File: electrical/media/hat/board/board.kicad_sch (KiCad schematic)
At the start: 9 parts, among them J101 RPI_PINS, J102 5V_IN, SW101 TS50810-411-02528

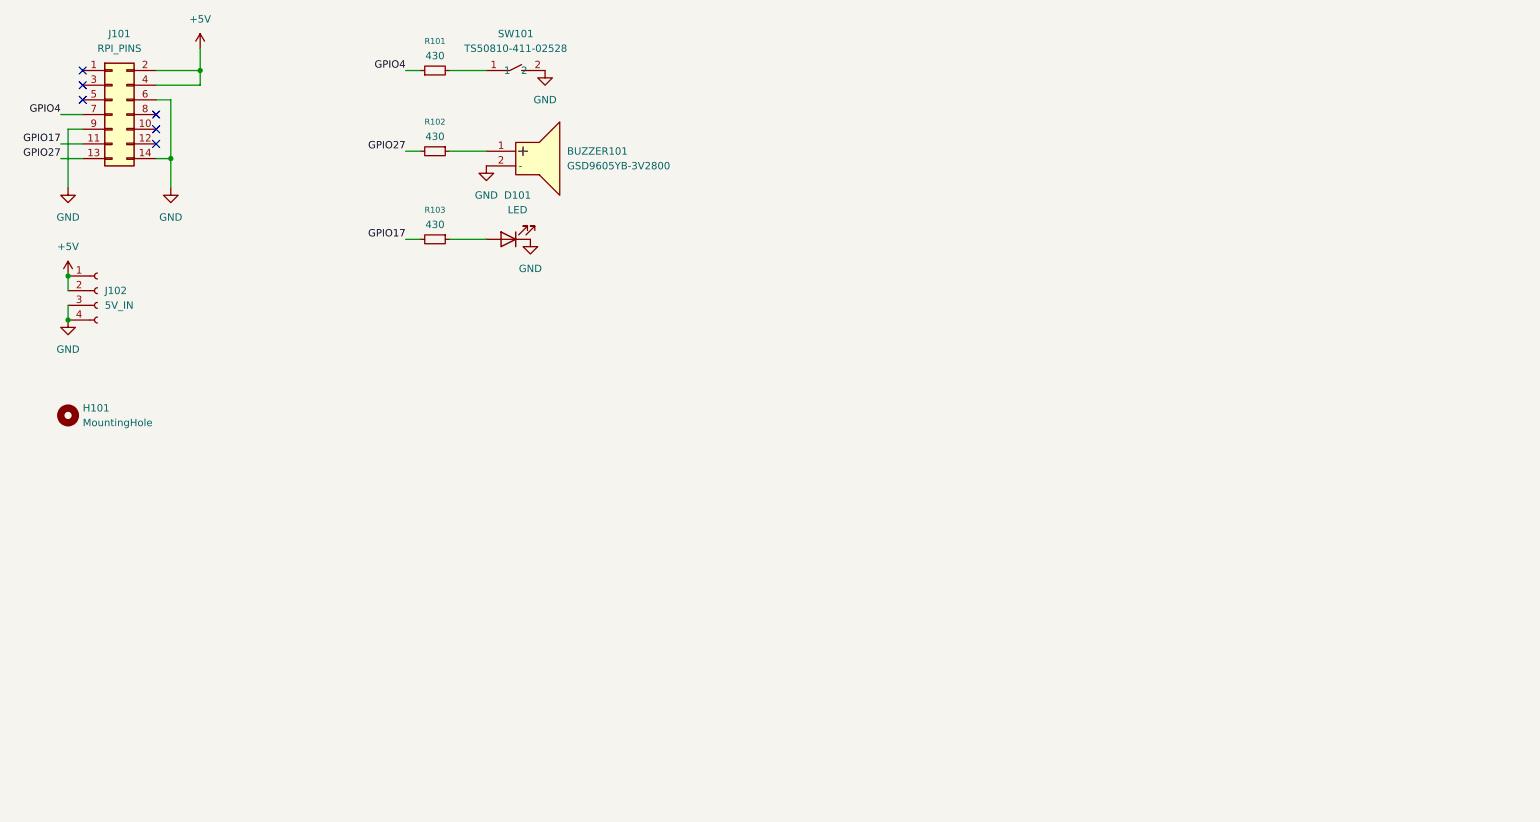
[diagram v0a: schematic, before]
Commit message: media hat power fix fabrication ready (#22)
* media hat power fix fabrication ready

* fix  STEP path

* flip connector polarity

* change FLT to RED LED

* LCSC number fix
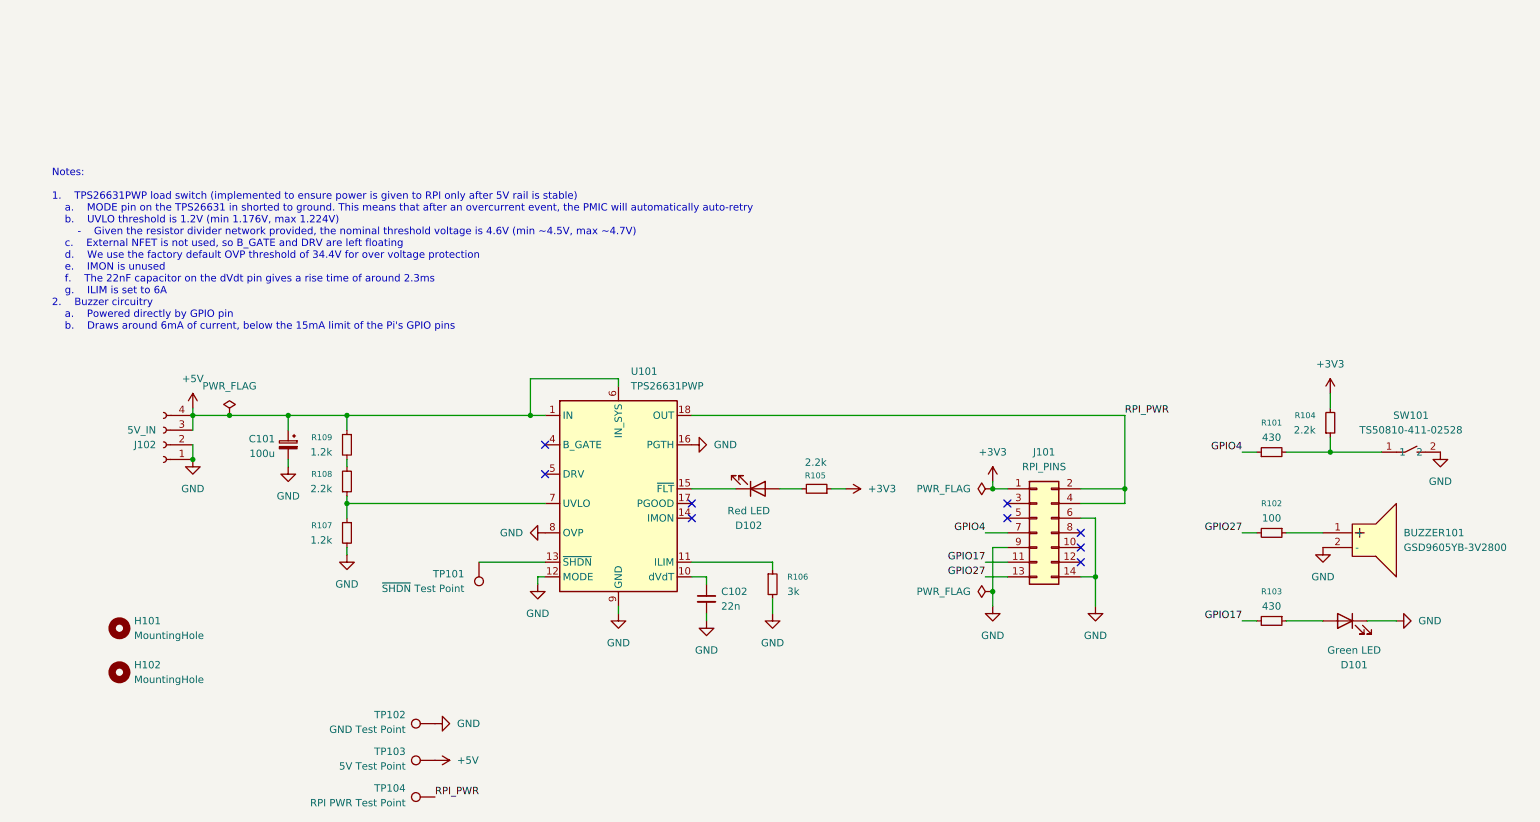
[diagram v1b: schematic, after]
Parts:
- added C101: 100u, Capacitor_Tantalum_SMD:CP_EIA-7343-31_Kemet-D, symbol Device:C_Polarized_Small
- added C102: 22n, Capacitor_SMD:C_0402_1005Metric, symbol Device:C_Small
- added D102: Red LED, LED_SMD:LED_0603_1608Metric, symbol Device:LED
- added H102: MountingHole, MountingHole:MountingHole_2.5mm, symbol Mechanical:MountingHole
- added R104, R105, R108: 2.2k, Resistor_SMD:R_0402_1005Metric, symbol Device:R_Small
- added R106: 3k, Resistor_SMD:R_0603_1608Metric, symbol Device:R_Small
- added R107, R109: 1.2k, Resistor_SMD:R_0402_1005Metric, symbol Device:R_Small
- added TP101: ~{SHDN} Test Point, TestPoint:TestPoint_Keystone_5015_Micro_Mini, symbol Connector:TestPoint
- added TP102: GND Test Point, TestPoint:TestPoint_Keystone_5015_Micro_Mini, symbol Connector:TestPoint
- added TP103: 5V Test Point, TestPoint:TestPoint_Keystone_5015_Micro_Mini, symbol Connector:TestPoint
- added TP104: RPI PWR Test Point, TestPoint:TestPoint_Keystone_5015_Micro_Mini, symbol Connector:TestPoint
- added U101: TPS26631PWP, Package_SO:HTSSOP-20-1EP_4.4x6.5mm_P0.65mm_EP3.4x6.5mm_Mask2.96x2.96mm_ThermalVias, symbol Power_Management:TPS26631PWP
- D101: value LED -> Green LED
- H101: footprint MountingHole:MountingHole_3.2mm_M3 -> MountingHole:MountingHole_2.5mm
- R102: value 430 -> 100; LCSC C137868 -> C25076
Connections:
- net +5V: now also J102.3 (Pin_3), J102.4 (Pin_4), C101.1, R109.1, TP103.1, U101.1 (IN), U101.2 (IN), U101.3 (IN), U101.6 (IN_SYS); no longer J101.2 (Pin_2), J101.4 (Pin_4), J102.1 (Pin_1), J102.2 (Pin_2)
- net GND: now also J102.1 (Pin_1), J102.2 (Pin_2), C101.2, C102.2, R106.2, R107.2, TP102.1, U101.12 (MODE), U101.16 (PGTH), U101.21 (GND), U101.8 (OVP), U101.9 (GND); no longer J102.3 (Pin_3), J102.4 (Pin_4)
- net at R101.2, SW101.1: now also R104.1
- net +3V3: now reaches J101.1 (Pin_1)
- net +3V3: now also R104.2, R105.1
- new net: R107.1, R108.1, U101.7 (UVLO)
- new net: R108.2, R109.2
- new net: C102.1, U101.10 (dVdT)
- new net: TP101.1, U101.13 (~{SHDN})
- new net: D102.1 (K), U101.15 (~{FLT})
- new net: D102.2 (A), R105.2
- new net: R106.1, U101.11 (ILIM)
- new net RPI_PWR: J101.2 (Pin_2), J101.4 (Pin_4), TP104.1, U101.18 (OUT), U101.19 (OUT), U101.20 (OUT)
- no-connect marks 6 -> 9
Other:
- note added: "Notes: 1. TPS26631PWP load switch (implemented to ensure power is given to RPI only after 5V rail is stable) a. MODE pin on the TPS26631 in shorted to ground. This means that after an overcurrent event, the PMIC will automatically auto-retry b. UVLO threshold is 1.2V (min 1.176V, max 1.224V) - Given the resistor divider network provided, the nominal threshold voltage is 4.6V (min ~4.5V, max ~4.7V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"
- moved on the sheet: BUZZER101, D101, H101, J101, R101, R102, R103, SW101
